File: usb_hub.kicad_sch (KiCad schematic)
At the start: 8 parts, among them U2 USB2514B_Bi, Y1 ABLS-24.000MHZ-B4-T

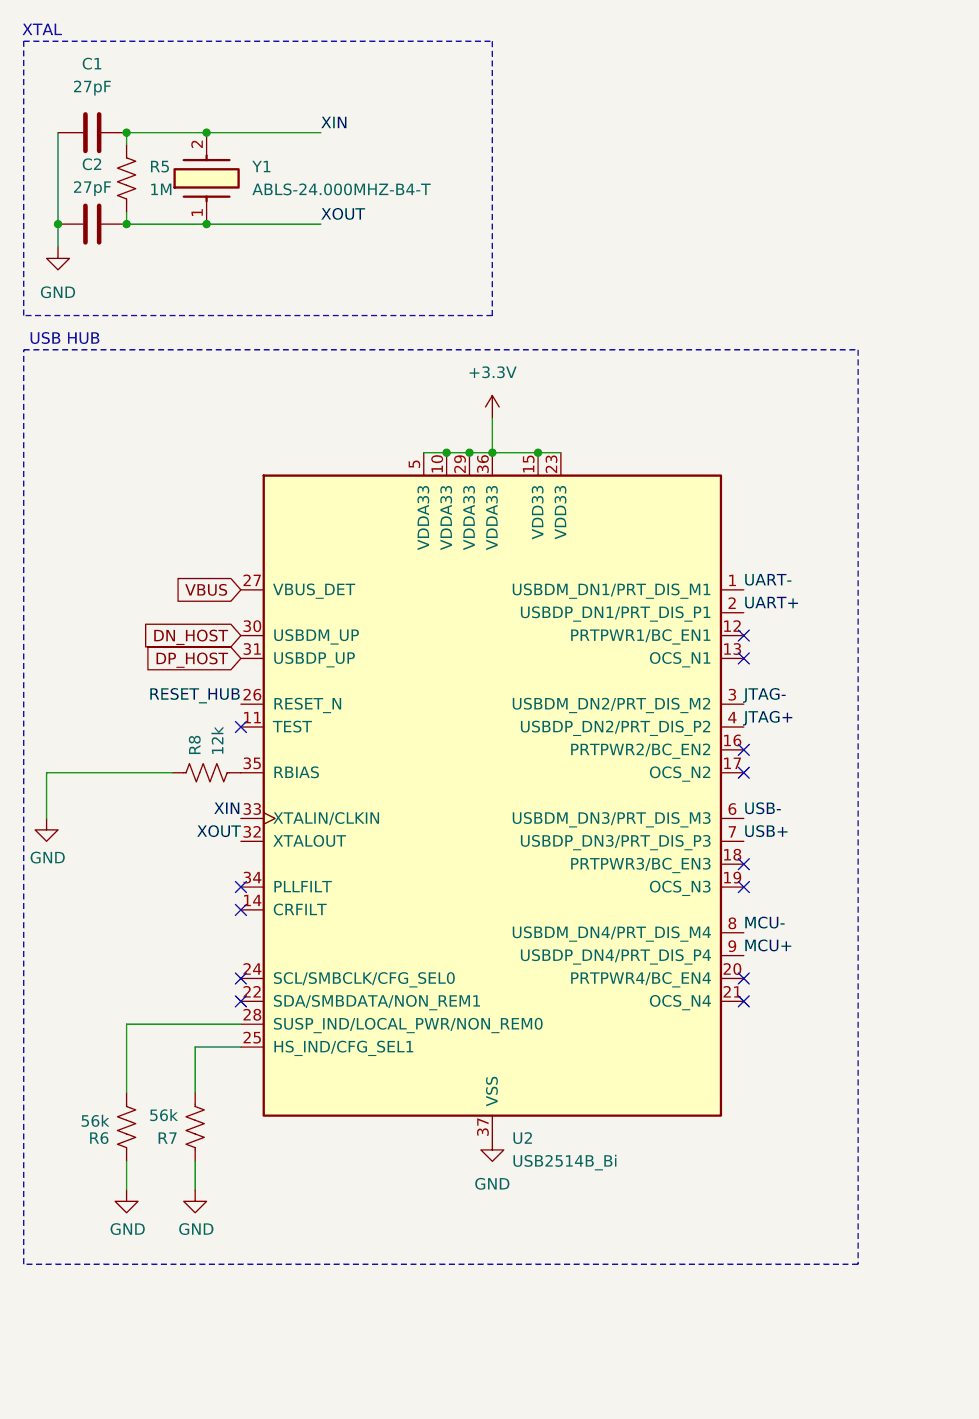
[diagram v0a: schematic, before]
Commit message: Used steppenprobe as base for our UART and JTAG.
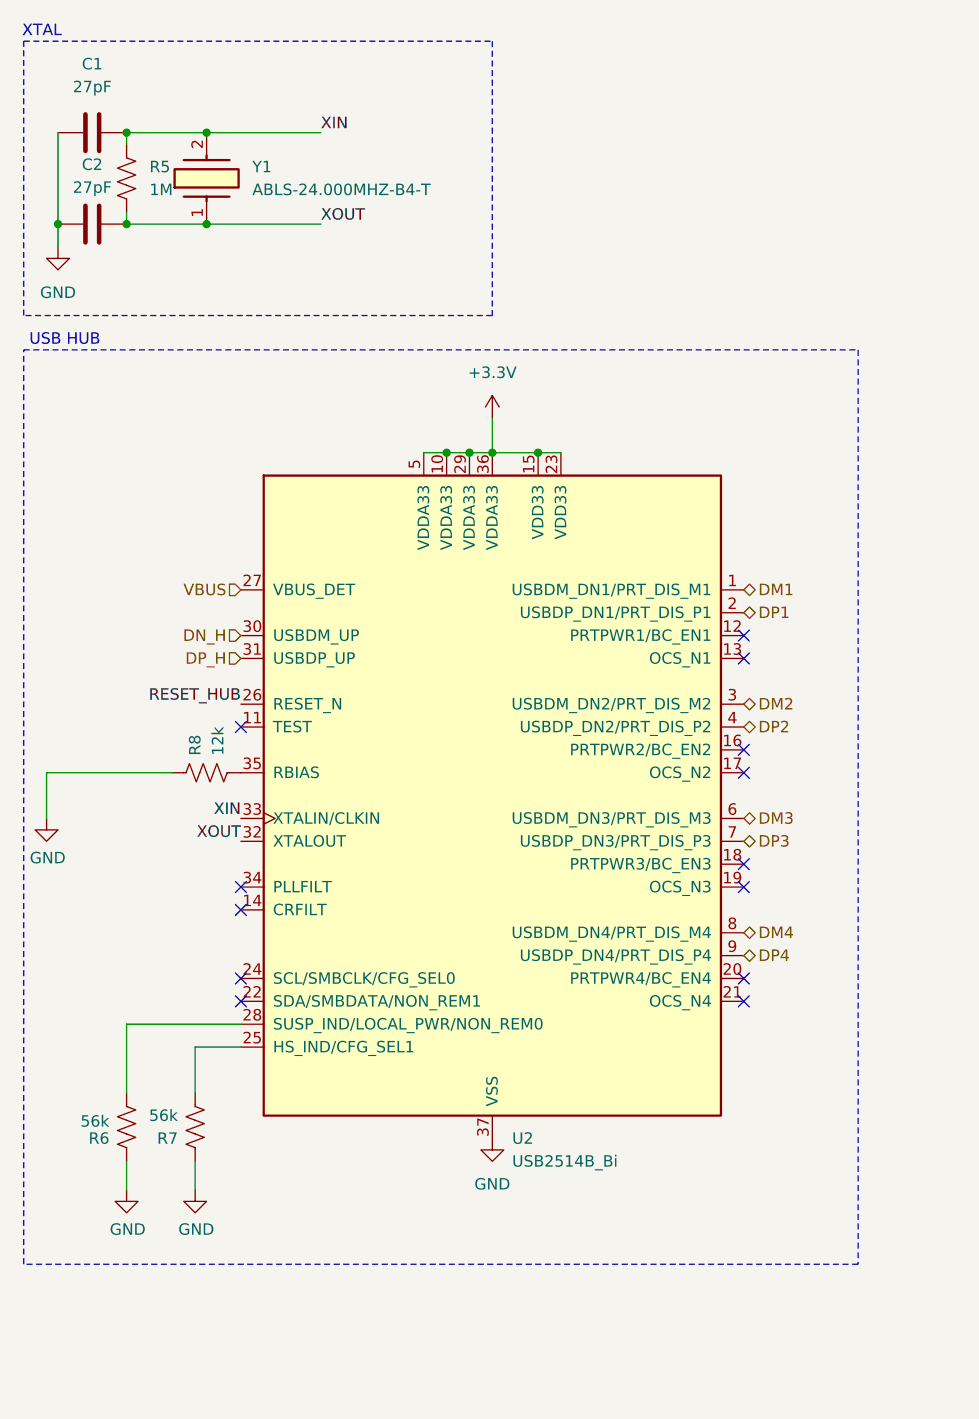
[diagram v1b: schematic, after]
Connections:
- net DN_HOST renamed DN_H
- net DP_HOST renamed DP_H
- net JTAG+ renamed DP2
- net JTAG- renamed DM2
- net MCU+ renamed DP4
- net MCU- renamed DM4
- net UART+ renamed DP1
- net UART- renamed DM1
- net USB+ renamed DP3
- net USB- renamed DM3
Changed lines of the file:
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@@
-		)
-	)
-	(label "UART+"
-		(at 93.98 80.01 0)
-		(fields_autoplaced yes)
-		(effects
-			(font
-				(size 1.27 1.27)
-			)
-			(justify left bottom)
 		)
 	)
 	(label "XIN"
 		(at 46.99 26.67 0)
-		(fields_autoplaced yes)
-		(effects
-			(font
-				(size 1.27 1.27)
-			)
-			(justify left bottom)
-		)
-	)
-	(label "JTAG-"
-		(at 93.98 90.17 0)
-		(fields_autoplaced yes)
-		(effects
-			(font
-				(size 1.27 1.27)
-			)
-			(justify left bottom)
-		)
-	)
-	(label "USB+"
-		(at 93.98 105.41 0)
-		(fields_autoplaced yes)
-		(effects
-			(font
-				(size 1.27 1.27)
-			)
-			(justify left bottom)
-		)
-	)
-	(label "MCU-"
-		(at 93.98 115.57 0)
 		(fields_autoplaced yes)
 		(effects
@@
 		)
 	)
-	(label "UART-"
-		(at 93.98 77.47 0)
-		(fields_autoplaced yes)
-		(effects
-			(font
-				(size 1.27 1.27)
-			)
-			(justify left bottom)
-		)
-	)
 	(label "RESET_HUB"
 		(at 38.1 90.17 180)
@@
 		)
 	)
-	(label "USB-"
-		(at 93.98 102.87 0)
-		(fields_autoplaced yes)
+	(hierarchical_label "DM2"
+		(shape bidirectional)
+		(at 93.98 90.17 0)
 		(effects
 			(font
 				(size 1.27 1.27)
 			)
-			(justify left bottom)
+			(justify left)
 		)
 	)
-	(label "MCU+"
-		(at 93.98 118.11 0)
-		(fields_autoplaced yes)
+	(hierarchical_label "DP1"
+		(shape bidirectional)
+		(at 93.98 80.01 0)
 		(effects
 			(font
 				(size 1.27 1.27)
 			)
-			(justify left bottom)
+			(justify left)
 		)
 	)
-	(label "JTAG+"
-		(at 93.98 92.71 0)
-		(fields_autoplaced yes)
+	(hierarchical_label "DP3"
+		(shape bidirectional)
+		(at 93.98 105.41 0)
 		(effects
 			(font
 				(size 1.27 1.27)
 			)
-			(justify left bottom)
+			(justify left)
 		)
 	)
-	(global_label "DN_HOST"
+	(hierarchical_label "DM4"
+		(shape bidirectional)
+		(at 93.98 115.57 0)
+		(effects
+			(font
+				(size 1.27 1.27)
+			)
+			(justify left)
+		)
+	)
+	(hierarchical_label "DM1"
+		(shape bidirectional)
+		(at 93.98 77.47 0)
+		(effects
+			(font
+				(size 1.27 1.27)
+			)
+			(justify left)
+		)
+	)
+	(hierarchical_label "DP2"
+		(shape bidirectional)
+		(at 93.98 92.71 0)
+		(effects
+			(font
+				(size 1.27 1.27)
+			)
+			(justify left)
+		)
+	)
+	(hierarchical_label "DM3"
+		(shape bidirectional)
+		(at 93.98 102.87 0)
+		(effects
+			(font
+				(size 1.27 1.27)
+			)
+			(justify left)
+		)
+	)
+	(hierarchical_label "DN_H"
 		(shape input)
 		(at 38.1 82.55 180)
@@
 			(justify right)
 		)
-		(property "Intersheetrefs" "${INTERSHEET_REFS}"
-			(at 26.7086 82.55 0)
-			(effects
-				(font
-					(size 1.27 1.27)
-				)
-				(justify right)
-				(hide yes)
+	)
+	(hierarchical_label "VBUS"
+		(shape input)
+		(at 38.1 77.47 180)
+		(fields_autoplaced yes)
+		(effects
+			(font
+				(size 1.27 1.27)
 			)
+			(justify right)
 		)
 	)
-	(global_label "DP_HOST"
+	(hierarchical_label "DP4"
+		(shape bidirectional)
+		(at 93.98 118.11 0)
+		(effects
+			(font
+				(size 1.27 1.27)
+			)
+			(justify left)
+		)
+	)
+	(hierarchical_label "DP_H"
 		(shape input)
 		(at 38.1 85.09 180)
@@
 			(justify right)
 		)
-		(property "Intersheetrefs" "${INTERSHEET_REFS}"
-			(at 26.7691 85.09 0)
-			(effects
-				(font
-					(size 1.27 1.27)
-				)
-				(justify right)
-				(hide yes)
-			)
-		)
 	)
-	(global_label "VBUS"
-		(shape input)
-		(at 38.1 77.47 180)
-		(fields_autoplaced yes)
-		(effects
-			(font
-				(size 1.27 1.27)
-			)
-			(justify right)
-		)
-		(property "Intersheetrefs" "${INTERSHEET_REFS}"
-			(at 30.2162 77.47 0)
-			(effects
-				(font
-					(size 1.27 1.27)
-				)
-				(justify right)
-				(hide yes)
-			)
-		)
-	)

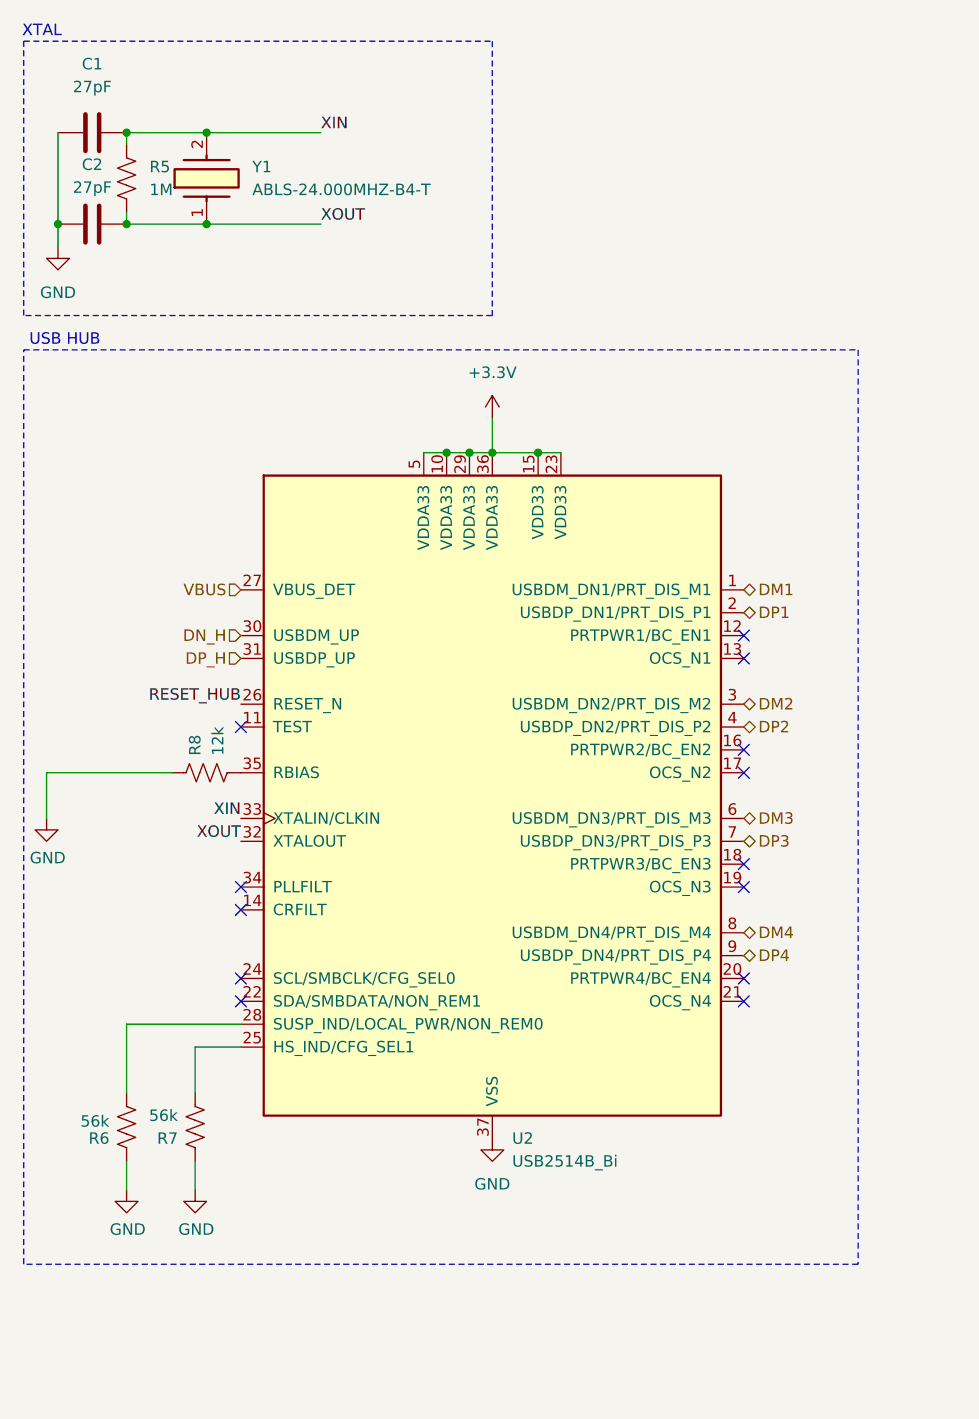
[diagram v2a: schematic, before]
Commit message: started pcb layout, host and usbhub done
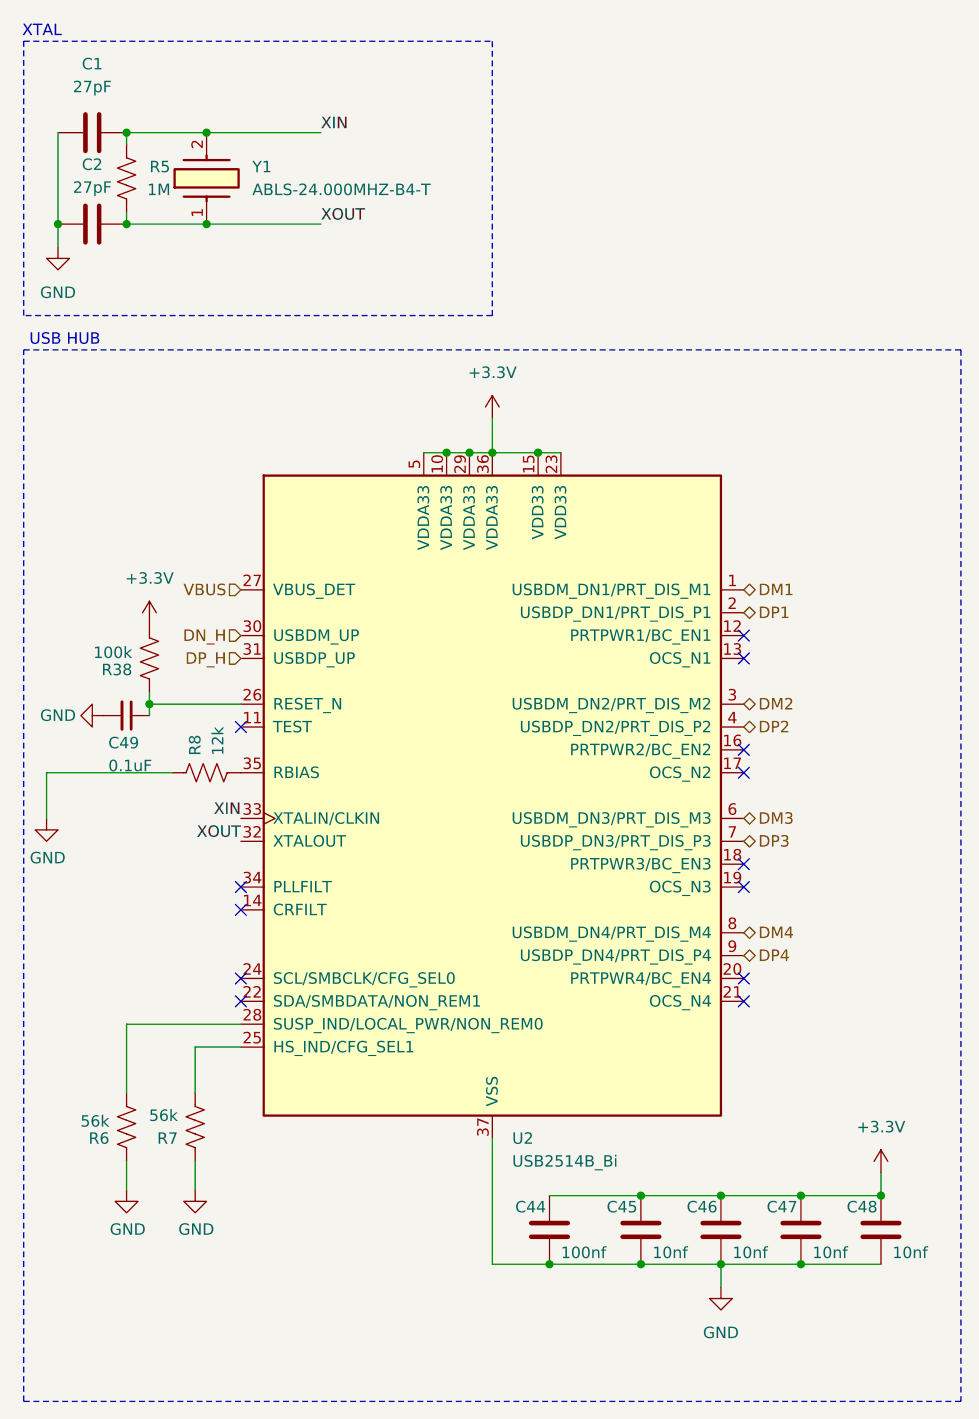
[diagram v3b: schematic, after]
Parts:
- added C44: 100nf, Capacitor_SMD:C_0603_1608Metric, symbol Device:C
- added C45, C46, C47, C48: 10nf, Capacitor_SMD:C_0603_1608Metric, symbol Device:C
- added C49: 0.1uF, Capacitor_SMD:C_0402_1005Metric, symbol Device:C_Small
- added R38: 100k, Resistor_SMD:R_0603_1608Metric, symbol Device:R_US
- C1, C2: footprint (none) -> Capacitor_SMD:C_0603_1608Metric
- R5: footprint (none) -> Resistor_SMD:R_0603_1608Metric
- R6, R7, R8: footprint Resistor_SMD:R_0805_2012Metric_Pad1.15x1.40mm_HandSolder -> Resistor_SMD:R_0603_1608Metric
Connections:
- net +3.3V: now also C44.1, C45.1, C46.1, C47.1, C48.1, R38.2
- net GND: now also C44.2, C45.2, C46.2, C47.2, C48.2, C49.2
- net RESET_HUB: no longer names the net of U2.26 (RESET_N)
- net RESET_HUB: now also C49.1, R38.1

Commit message: routed stm32
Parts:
- removed Y1: ABLS-24.000MHZ-B4-T, ABLS24000MHZB4T, symbol SamacSys_Parts:ABLS-24.000MHZ-B4-T
- added Y3: ABM3B-24.000MHZ-B2-T, ABM3B, symbol SamacSys_Parts:ABM3B-24.000MHZ-B2-T
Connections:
- net GND: now also Y3.2 (GND_1), Y3.4 (GND_2)
- net XIN: now also Y3.3 (XTAL_2)
- net XOUT: now also Y3.1 (XTAL_1)
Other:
- moved on the sheet: C2, R5

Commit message: pcb routed!!!!!!!
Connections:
- net DM1: now also U2.6 (USBDM_DN3/PRT_DIS_M3); no longer U2.1 (USBDM_DN1/PRT_DIS_M1)
- net DM3: now also U2.8 (USBDM_DN4/PRT_DIS_M4); no longer U2.6 (USBDM_DN3/PRT_DIS_M3)
- net DM4: now also U2.1 (USBDM_DN1/PRT_DIS_M1); no longer U2.8 (USBDM_DN4/PRT_DIS_M4)
- net DP1: now also U2.7 (USBDP_DN3/PRT_DIS_P3); no longer U2.2 (USBDP_DN1/PRT_DIS_P1)
- net DP3: now also U2.9 (USBDP_DN4/PRT_DIS_P4); no longer U2.7 (USBDP_DN3/PRT_DIS_P3)
- net DP4: now also U2.2 (USBDP_DN1/PRT_DIS_P1); no longer U2.9 (USBDP_DN4/PRT_DIS_P4)
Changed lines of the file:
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@@
+		)
+	)
+	(hierarchical_label "DP1"
+		(shape bidirectional)
+		(at 93.98 105.41 0)
+		(fields_autoplaced yes)
+		(effects
+			(font
+				(size 1.27 1.27)
+			)
+			(justify left)
 		)
 	)
@@
 		)
 	)
-	(hierarchical_label "DP1"
+	(hierarchical_label "DP3"
 		(shape bidirectional)
-		(at 93.98 80.01 0)
+		(at 93.98 118.11 0)
 		(fields_autoplaced yes)
 		(effects
@@
 		)
 	)
-	(hierarchical_label "DP3"
+	(hierarchical_label "DP4"
 		(shape bidirectional)
-		(at 93.98 105.41 0)
-		(fields_autoplaced yes)
-		(effects
-			(font
-				(size 1.27 1.27)
-			)
-			(justify left)
-		)
-	)
-	(hierarchical_label "DM4"
-		(shape bidirectional)
-		(at 93.98 115.57 0)
-		(fields_autoplaced yes)
-		(effects
-			(font
-				(size 1.27 1.27)
-			)
-			(justify left)
-		)
-	)
-	(hierarchical_label "DM1"
-		(shape bidirectional)
-		(at 93.98 77.47 0)
+		(at 93.98 80.01 0)
 		(fields_autoplaced yes)
 		(effects
@@
 		)
 	)
-	(hierarchical_label "DM3"
+	(hierarchical_label "DM1"
 		(shape bidirectional)
 		(at 93.98 102.87 0)
@@
 		)
 	)
-	(hierarchical_label "DP4"
-		(shape bidirectional)
-		(at 93.98 118.11 0)
-		(fields_autoplaced yes)
-		(effects
-			(font
-				(size 1.27 1.27)
-			)
-			(justify left)
-		)
-	)
 	(hierarchical_label "DP_H"
 		(shape input)
@@
 		)
 	)
+	(hierarchical_label "DM3"
+		(shape bidirectional)
+		(at 93.98 115.57 0)
+		(fields_autoplaced yes)
+		(effects
+			(font
+				(size 1.27 1.27)
+			)
+			(justify left)
+		)
+	)
+	(hierarchical_label "DM4"
+		(shape bidirectional)
+		(at 93.98 77.47 0)
+		(fields_autoplaced yes)
+		(effects
+			(font
+				(size 1.27 1.27)
+			)
+			(justify left)
+		)
+	)
